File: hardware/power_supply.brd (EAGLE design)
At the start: 76.2 x 38.1 mm, 29 parts, among them Q1 IRF630N, U1 MC34063

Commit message: Updating power supply 7/10
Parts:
- moved JP1 1.02 mm to (61.5, 34.3)
- moved JP2 0.51 mm to (71.9, 9.40)
- renumbered U$7 to U2, U$8 to D3
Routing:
- net +5V: track 53.0 -> 51.5 mm
- net STCP: track 29.0 -> 28.2 mm
- net SHCP: track 25.4 -> 24.6 mm
- net DI: track 26.2 -> 25.4 mm
- net +3V3: track 40.8 -> 40.2 mm
- net GND: track 1.52 -> 1.02 mm
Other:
- board text added: "3V3"
- board text added: "5V"
- board text added: "GND"
- board text added: "L1"
- board text added: "L2"
- board text added: "POS"
- board text added: "SD"
- board text added: "SHCP"
- board text added: "STCP"
- board text added: "https://github.com/bmboucher/nixie_ticker"

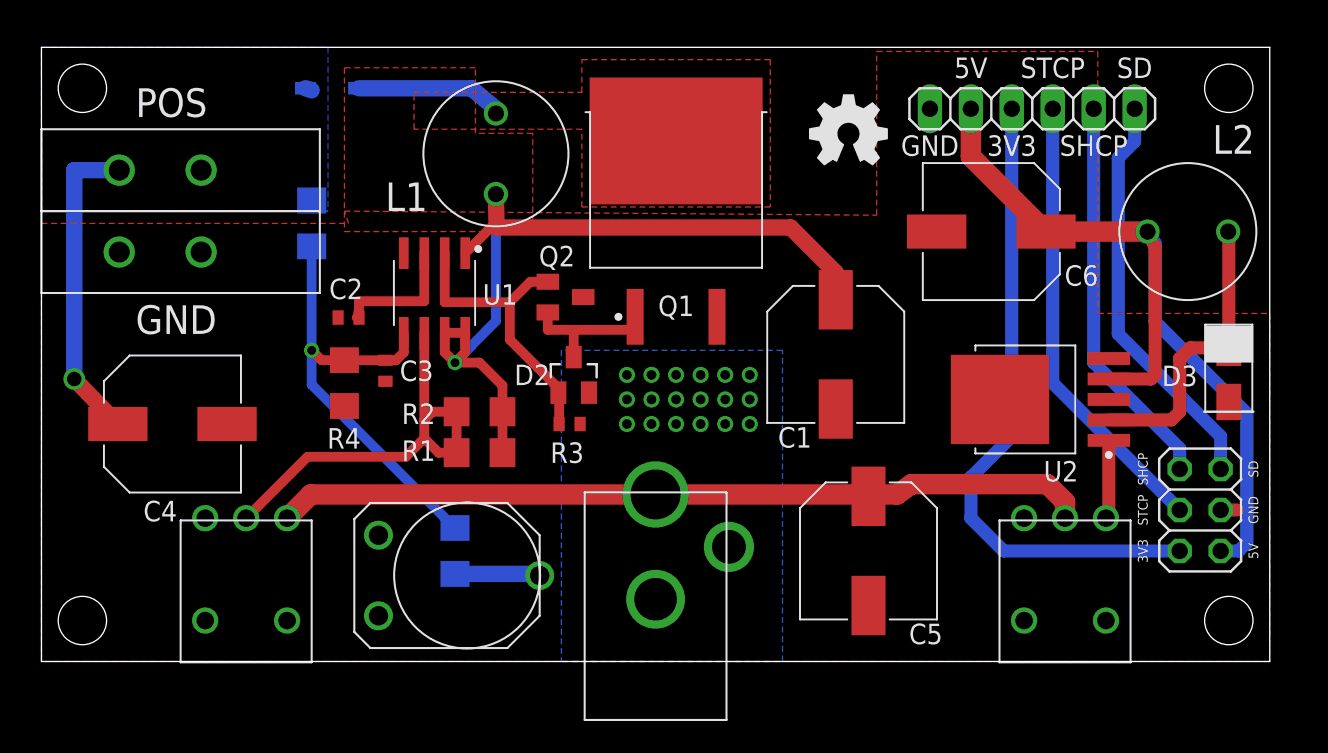
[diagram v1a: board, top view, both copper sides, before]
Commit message: Updating power_supply, 7-11
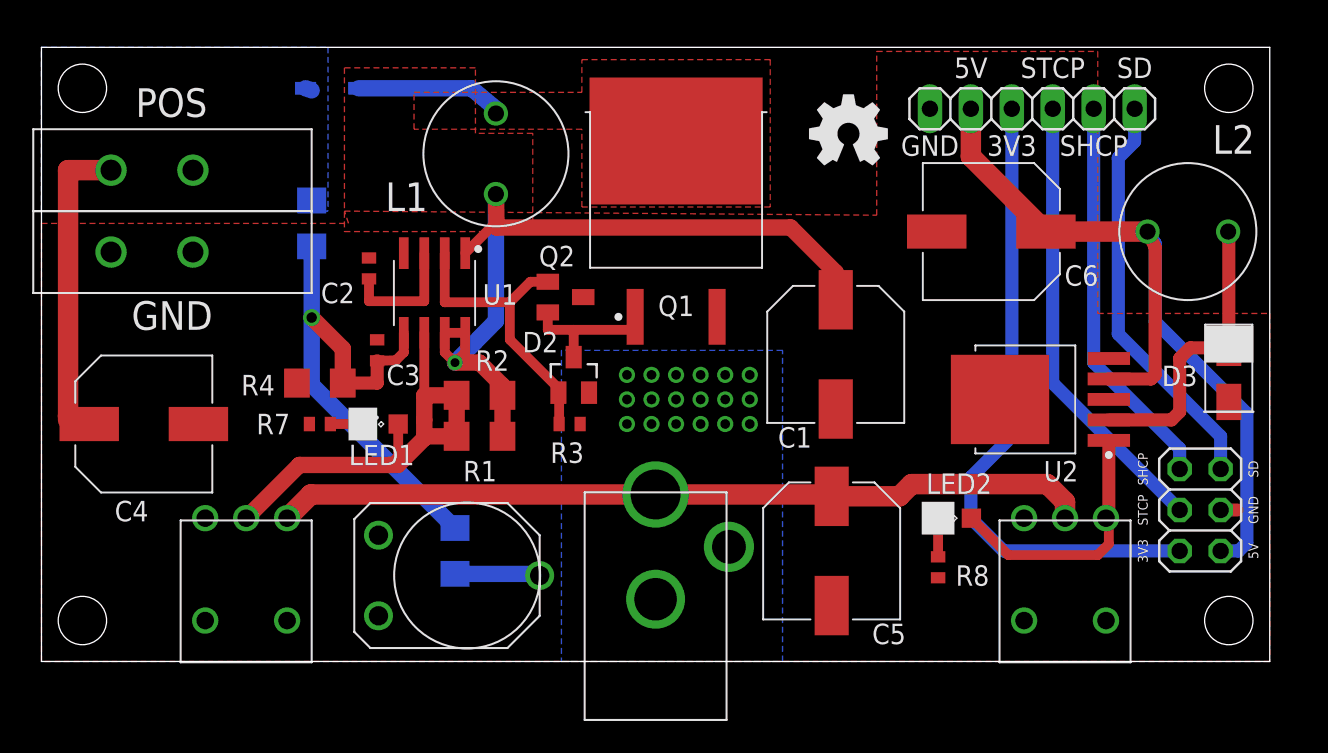
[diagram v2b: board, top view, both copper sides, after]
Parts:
- added LED1, LED2: (no value), led:SML0805
- added R7, R8: 1k, resistor:R0402
- moved C2 3.30 mm to (20.3, 24.4), turned to 90 degrees
- moved C5 2.29 mm to (49.0, 6.86)
- moved C4 1.78 mm to (6.35, 14.7)
- moved R4 1.52 mm to (17.3, 17.3), turned to 0 degrees
- moved C3 1.37 mm to (20.8, 19.3), turned to 90 degrees
- moved R2 1.02 mm to (27.2, 16.5)
- moved R1 1.02 mm to (27.2, 14.0)
- moved U$5 0.51 mm to (4.32, 30.5)
- moved U$6 0.51 mm to (4.32, 25.4)
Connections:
- new net N$11: LED1.C, R7.2
- new net N$12: LED2.C, R8.2
- net GND: now also R7.1, R8.1
- net N$6: now also LED1.A
- net N$8: now also LED2.A
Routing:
- net N$8: track 4.90 -> 16.4 mm
- net N$6: track 26.8 -> 30.5 mm
- net N$9: track 29.2 -> 32.6 mm
- net N$12: track 0.00 -> 2.41 mm
- net N$11: track 0.00 -> 2.11 mm
- net V+: vias 1 -> 0

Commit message: Updating power_supply
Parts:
- moved R8 7.47 mm to (57.9, 13.0), turned to 0 degrees
- moved LED2 6.31 mm to (61.5, 13.0)
- moved U2 1.78 mm to (62.0, 18.0)
- moved R1 1.37 mm to (26.7, 15.2)
- moved R2 1.37 mm to (26.7, 17.8)
- moved R3 0.80 mm to (32.5, 14.0), turned to 90 degrees
- moved D2 0.41 mm to (33.4, 17.8)
- moved Q2 0.25 mm to (32.5, 22.4), turned to 0 degrees
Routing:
- net N$1: track 53.2 -> 45.3 mm, vias 1 -> 0
- net N$8: track 16.4 -> 10.4 mm
- net N$2: track 9.26 -> 14.6 mm
- net N$10: track 18.4 -> 15.8 mm
- net +5V: track 51.5 -> 48.8 mm
- net N$6: track 30.5 -> 27.9 mm
- net N$5: track 9.09 -> 6.63 mm
- net N$9: track 32.6 -> 31.0 mm
- net N$4: track 18.8 -> 17.4 mm, vias 0 -> 2
- net N$12: track 2.41 -> 1.86 mm
- net GND: vias 18 -> 22

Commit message: Updating 8-12
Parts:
- removed JP1: (no value), pinhead:1X06
- removed LED1: (no value), led:SML0805
- added C7, C8: (no value), resistor:C0402
- added F1, F2: FUSE_1206, nixie_ticker:R1206
- added HV: (no value), led:SML0805
- added JP3: (no value), pinhead:1X05
- added U3: CD40109B_SPLITEN, nixie_ticker:SOP65P640X120-16
- C1, C5, C6: value UUR1C221MCL6GS -> 220uF
- C2: value (none) -> 680pF
- C3: value (none) -> 0.01uF
- C4: value UUR1C221MCL6GS -> 3.3uF
- D1: value BAV21W -> (none)
- D2: value MMBD914L -> (none)
- L1: value RLB9012 -> 100uH
- R3: device resistor:R0402 -> resistor:R0805
- R7, R8: value 1k -> 2k; device resistor:R0402 -> resistor:R0805
- RX: value 3309P-1-202 -> 2k
- moved D1 2.34 mm to (18.6, 33.3)
- moved L1 1.65 mm to (26.5, 31.5), turned to 225 degrees
- moved R8 1.27 mm to (56.6, 13.0)
- moved R3 1.00 mm to (33.5, 14.2), turned to 180 degrees
- moved R7 0.57 mm to (16.8, 14.5)
- renumbered LED2 to LOGIC, U$2 to RX, U$3 to SW1, U$4 to SW2, U$9 to L2
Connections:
- removed net DI: JP1.6, JP2.2
- removed net SHCP: JP1.5, JP2.1
- removed net STCP: JP1.4, JP2.3
- new net CLK_H: JP3.4, U3.11
- new net CLK_L: JP2.1, U3.10
- new net DATA_H: JP3.5, U3.5
- new net DATA_L: JP2.2, U3.14
- new net LATCH_H: JP3.3, U3.13
- new net LATCH_L: JP2.3, U3.6
- new net N$13: F1.2, SW2.P$2, SW2.P$3
- new net N$14: F2.2, SW1.P$1
- net +12V: now also F1.1, F2.1; no longer SW1.P$1, SW2.P$2
- net +3V3: now also C7.1, U3.1, U3.15, U3.7, U3.9; no longer JP1.3
- net +5V: now also C8.1, JP3.2, U3.16; no longer JP1.2
- net GND: now also C7.2, C8.2, JP3.1, U3.12, U3.2, U3.3, U3.4, U3.8; no longer JP1.1
- net N$11: now also HV.C; no longer LED1.C
- net N$6: now also HV.A; no longer LED1.A
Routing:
- net +3V3: track 40.2 -> 76.8 mm
- net STCP: track 28.2 -> 0.00 mm
- net CLK_L: track 0.00 -> 26.9 mm
- net GND: track 1.02 -> 27.5 mm, vias 22 -> 65
- net DI: track 25.4 -> 0.00 mm
- net LATCH_L: track 0.00 -> 25.3 mm
- net SHCP: track 24.6 -> 0.00 mm
- net DATA_L: track 0.00 -> 23.8 mm
- net +12V: track 50.7 -> 27.6 mm
- net DATA_H: track 0.00 -> 17.5 mm
- net N$14: track 0.00 -> 12.9 mm
- net +5V: track 48.8 -> 55.5 mm
- net N$13: track 0.00 -> 6.27 mm
- net CLK_H: track 0.00 -> 5.28 mm
- net LATCH_H: track 0.00 -> 4.76 mm
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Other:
- board text added: "C"
- board text added: "D"
- board text added: "L"
- board text removed: "SD"
- board text removed: "SHCP"
- board text removed: "STCP"

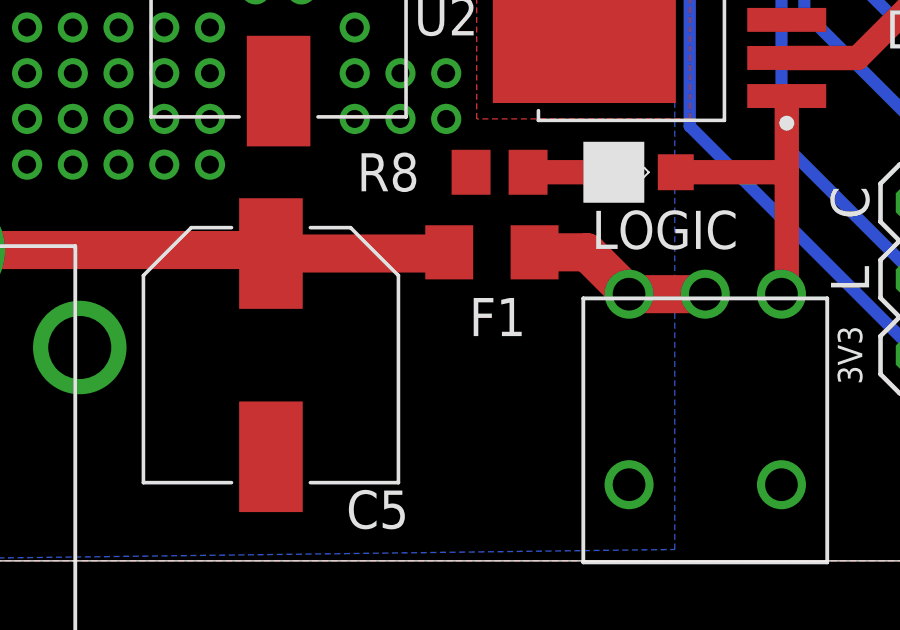
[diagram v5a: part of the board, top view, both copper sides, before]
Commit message: Updates to BOM
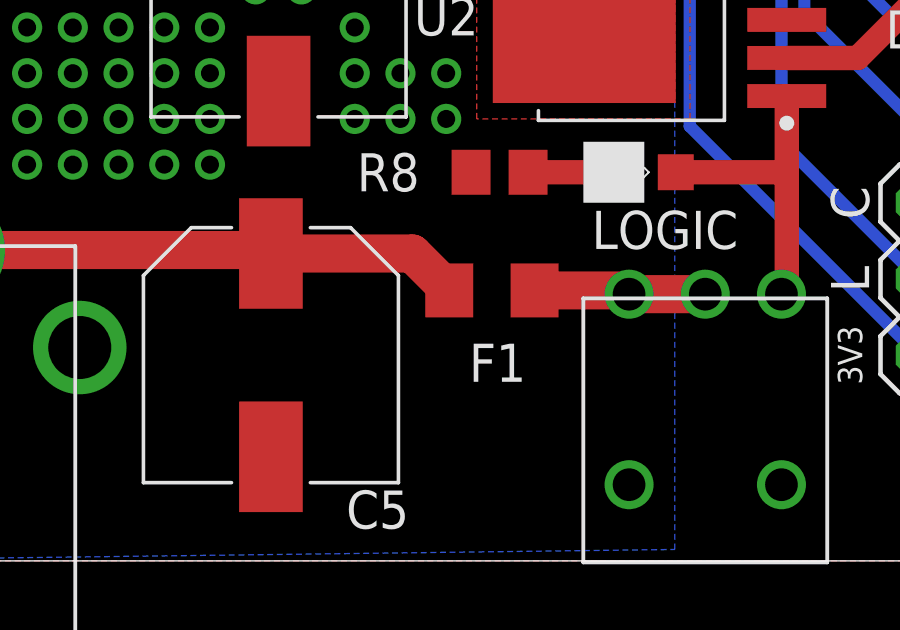
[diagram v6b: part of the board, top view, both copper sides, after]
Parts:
- moved F1 1.27 mm to (56.4, 9.02)
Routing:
- net N$13: track 6.27 -> 5.74 mm
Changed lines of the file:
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@@
 <grid distance="10" unitdist="mil" unit="mil" style="lines" multiple="1" display="yes" altdistance="5" altunitdist="mil" altunit="mil"/>
 <layers>
-<layer number="1" name="Top" color="4" fill="1" visible="yes" active="yes"/>
+<layer number="1" name="Top" color="4" fill="1" visible="no" active="yes"/>
 <layer number="16" name="Bottom" color="1" fill="1" visible="yes" active="yes"/>
 <layer number="17" name="Pads" color="2" fill="1" visible="yes" active="yes"/>
@@
 <layer number="19" name="Unrouted" color="6" fill="1" visible="yes" active="yes"/>
 <layer number="20" name="Dimension" color="24" fill="1" visible="yes" active="yes"/>
-<layer number="21" name="tPlace" color="7" fill="1" visible="yes" active="yes"/>
+<layer number="21" name="tPlace" color="7" fill="1" visible="no" active="yes"/>
 <layer number="22" name="bPlace" color="7" fill="1" visible="yes" active="yes"/>
-<layer number="23" name="tOrigins" color="15" fill="1" visible="yes" active="yes"/>
+<layer number="23" name="tOrigins" color="15" fill="1" visible="no" active="yes"/>
 <layer number="24" name="bOrigins" color="15" fill="1" visible="yes" active="yes"/>
-<layer number="25" name="tNames" color="7" fill="1" visible="yes" active="yes"/>
+<layer number="25" name="tNames" color="7" fill="1" visible="no" active="yes"/>
 <layer number="26" name="bNames" color="7" fill="1" visible="yes" active="yes"/>
 <layer number="27" name="tValues" color="7" fill="1" visible="no" active="yes"/>
@@
 <layer number="37" name="tTest" color="7" fill="1" visible="no" active="yes"/>
 <layer number="38" name="bTest" color="7" fill="1" visible="no" active="yes"/>
-<layer number="39" name="tKeepout" color="4" fill="11" visible="yes" active="yes"/>
+<layer number="39" name="tKeepout" color="4" fill="11" visible="no" active="yes"/>
 <layer number="40" name="bKeepout" color="1" fill="11" visible="yes" active="yes"/>
-<layer number="41" name="tRestrict" color="4" fill="10" visible="yes" active="yes"/>
+<layer number="41" name="tRestrict" color="4" fill="10" visible="no" active="yes"/>
 <layer number="42" name="bRestrict" color="1" fill="10" visible="yes" active="yes"/>
 <layer number="43" name="vRestrict" color="2" fill="10" visible="no" active="yes"/>
@@
 <layer number="48" name="Document" color="7" fill="1" visible="no" active="yes"/>
 <layer number="49" name="Reference" color="7" fill="1" visible="no" active="yes"/>
-<layer number="51" name="tDocu" color="7" fill="1" visible="yes" active="yes"/>
+<layer number="51" name="tDocu" color="7" fill="1" visible="no" active="yes"/>
 <layer number="52" name="bDocu" color="7" fill="1" visible="yes" active="yes"/>
 <layer number="88" name="SimResults" color="9" fill="1" visible="no" active="no"/>
@@
 </layers>
 <board>
-<fusionsync huburn="a.cGVyc29uYWw6dWUyYTY5OTEw" projecturn="a.cGVyc29uYWw6dWUyYTY5OTEwIzIwMTgwNjMwMTM4MzExNzgx" f3durn="urn:adsk.wipprod:dm.lineage:bjyJQ3K9ReGs7_9rgABCYQ" pcbguid="75b782bf-6294-4662-834a-dbb7a3b1e7c4" lastpulledtime="" lastsyncedchangeguid="92a7509f-8092-85b7-5944-d73b82e3d907"/>
+<fusionsync huburn="a.cGVyc29uYWw6dWUyYTY5OTEw" projecturn="a.cGVyc29uYWw6dWUyYTY5OTEwIzIwMTgwNjMwMTM4MzExNzgx" f3durn="urn:adsk.wipprod:dm.lineage:bjyJQ3K9ReGs7_9rgABCYQ" pcbguid="75b782bf-6294-4662-834a-dbb7a3b1e7c4" lastpulledtime="" lastsyncedchangeguid="4e2e07e8-fec4-d907-bfe8-be7f48e4bd99"/>
 <plain>
 <wire x1="0" y1="0" x2="76.2" y2="0" width="0" layer="20"/>
@@
 <attribute name="VALUE" x="56.007" y="11.049" size="1.27" layer="27"/>
 </element>
-<element name="F1" library="nixie_ticker" library_urn="urn:adsk.eagle:library:3857935" package="R1206" package3d_urn="urn:adsk.eagle:package:23540/2" value="FUSE_1206" x="56.388" y="10.287" smashed="yes">
-<attribute name="NAME" x="55.626" y="7.493" size="1.27" layer="25" font="vector"/>
-<attribute name="VALUE" x="55.118" y="7.747" size="1.27" layer="27"/>
+<element name="F1" library="nixie_ticker" library_urn="urn:adsk.eagle:library:3857935" package="R1206" package3d_urn="urn:adsk.eagle:package:23540/2" value="FUSE_1206" x="56.388" y="9.017" smashed="yes">
+<attribute name="NAME" x="55.626" y="5.969" size="1.27" layer="25" font="vector"/>
+<attribute name="VALUE" x="55.118" y="6.477" size="1.27" layer="27"/>
 </element>
 <element name="F2" library="nixie_ticker" library_urn="urn:adsk.eagle:library:3857935" package="R1206" package3d_urn="urn:adsk.eagle:package:23540/2" value="FUSE_1206" x="27.432" y="12.446" smashed="yes" rot="R180">
@@
 <wire x1="48.9057" y1="10.362" x2="49.022" y2="10.2457" width="1.27" layer="1"/>
 <contactref element="F1" pad="1"/>
-<wire x1="49.022" y1="10.2457" x2="54.9247" y2="10.2457" width="1.27" layer="1"/>
-<wire x1="54.9247" y1="10.2457" x2="54.966" y2="10.287" width="1.27" layer="1"/>
+<wire x1="49.022" y1="10.2457" x2="53.7373" y2="10.2457" width="1.27" layer="1"/>
+<wire x1="54.966" y1="9.017" x2="53.7373" y2="10.2457" width="1.27" layer="1"/>
 <contactref element="F2" pad="1"/>
 <wire x1="28.854" y1="11.43" x2="29.922" y2="10.362" width="1.27" layer="1"/>
@@
 <contactref element="F1" pad="2"/>
 <contactref element="SW2" pad="P$3"/>
-<wire x1="57.81" y1="10.287" x2="59.563" y2="10.287" width="1.27" layer="1"/>
-<wire x1="59.563" y1="10.287" x2="60.96" y2="8.89" width="1.27" layer="1"/>
+<wire x1="57.81" y1="9.017" x2="60.833" y2="9.017" width="1.27" layer="1"/>
+<wire x1="60.833" y1="9.017" x2="60.96" y2="8.89" width="1.27" layer="1"/>
 <wire x1="60.96" y1="8.89" x2="63.5" y2="8.89" width="1.27" layer="1"/>
 </signal>

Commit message: Final update before submitting to PCB shop
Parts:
- RX: device nixie_ticker:3309P-1-202 -> nixie_ticker:TC33X-2
- U2: value AP1507 -> AP1507SOIC-8; device nixie_ticker:TO127P990X239-6 -> nixie_ticker:SOIC127P600X175-8
- moved R6 2.67 mm to (23.0, 6.99)
- moved RX 1.55 mm to (24.4, 5.59), turned to 90 degrees
- moved R7 0.76 mm to (16.0, 14.5)
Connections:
- net +5V: now also U2.3; no longer U2.4
- net GND: now also U2.4, U2.7, U2.8; no longer U2.3
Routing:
- net N$8: track 10.4 -> 12.8 mm
- net N$10: track 15.8 -> 17.3 mm
- net GND: track 27.5 -> 26.0 mm
- net N$9: track 31.3 -> 30.1 mm
- net +5V: track 55.5 -> 56.5 mm
- net N$11: track 2.32 -> 3.08 mm
- net N$3: track 5.30 -> 5.29 mm, vias 0 -> 1
